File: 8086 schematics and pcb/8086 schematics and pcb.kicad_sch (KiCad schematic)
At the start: 0 parts

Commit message: first test of schmatic bus and PCB concept
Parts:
- added BUS1: 8086 BUS, Package_DIP:SMDIP-64_W15.24mm, symbol 8086PC:8086PC_BUS
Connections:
- new net AD0: BUS1.1 (AD0)
- new net AD1: BUS1.2 (AD1)
- new net AD2: BUS1.3 (AD2)
- new net AD3: BUS1.4 (AD3)
- new net AD4: BUS1.5 (AD4)
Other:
- added sheet 8086 Module (module_8086.kicad_sch)
- added sheet IO Module (module_io.kicad_sch)
- added sheet Microcontroller Module (module_microcontroller.kicad_sch)
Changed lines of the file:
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@@
     (date "2023.08.23")
   )
-  (bus_alias "8086BUS" (members "V_{CC}" "GND" "ADDRESS_LATCHED[0..19]" "DATA[0..15]"))
+  (bus_alias "8086BUS" (members "5V" "GND" "3V3" "AD[0..15]" "A[16..19]" "~{RD}" "~{WR}" "~{BHE}" "ALE" "CLK" "RESET" "HLDA" "HLDA" "~{INTA}" "INTR" "NMI" "~{TEST}" "READY" "~{IO[0..7]}" "~{SEG[2..7]}"))
+  (bus_entry (at 127 35.56) (size 2.54 -2.54)
+    (stroke (width 0) (type default))
+  )
+  (bus_entry (at 127 45.72) (size 2.54 -2.54)
+    (stroke (width 0) (type default))
+  )
+  (bus_entry (at 127 38.1) (size 2.54 -2.54)
+    (stroke (width 0) (type default))
+  )
+  (bus_entry (at 127 40.64) (size 2.54 -2.54)
+    (stroke (width 0) (type default))
+  )
+  (bus_entry (at 127 48.26) (size 2.54 -2.54)
+    (stroke (width 0) (type default))
+  )
+  (wire (pts (xy 137.16 35.56) (xy 137.16 33.02))
+    (stroke (width 0) (type default))
+  )
+  (wire (pts (xy 129.54 43.18) (xy 137.16 43.18))
+    (stroke (width 0) (type default))
+  )
+  (wire (pts (xy 129.54 45.72) (xy 137.16 45.72))
+    (stroke (width 0) (type default))
+  )
+  (bus (pts (xy 170.18 102.87) (xy 173.99 102.87))
+    (stroke (width 0) (type default))
+  )
+  (wire (pts (xy 132.08 38.1) (xy 132.08 40.64))
+    (stroke (width 0) (type default))
+  )
+  (bus (pts (xy 127 40.64) (xy 127 45.72))
+    (stroke (width 0) (type default))
+  )
+  (wire (pts (xy 129.54 35.56) (xy 134.62 35.56))
+    (stroke (width 0) (type default))
+  )
+  (bus (pts (xy 127 45.72) (xy 127 48.26))
+    (stroke (width 0) (type default))
+  )
+  (bus (pts (xy 127 48.26) (xy 127 121.92))
+    (stroke (width 0) (type default))
+  )
+  (wire (pts (xy 134.62 35.56) (xy 134.62 38.1))
+    (stroke (width 0) (type default))
+  )
+  (bus (pts (xy 127 38.1) (xy 127 40.64))
+    (stroke (width 0) (type default))
+  )
+  (bus (pts (xy 127 25.4) (xy 127 35.56))
+    (stroke (width 0) (type default))
+  )
+  (bus (pts (xy 170.18 25.4) (xy 127 25.4))
+    (stroke (width 0) (type default))
+  )
+  (bus (pts (xy 170.18 102.87) (xy 170.18 25.4))
+    (stroke (width 0) (type default))
+  )
+  (wire (pts (xy 129.54 33.02) (xy 137.16 33.02))
+    (stroke (width 0) (type default))
+  )
+  (bus (pts (xy 127 35.56) (xy 127 38.1))
+    (stroke (width 0) (type default))
+  )
+  (wire (pts (xy 134.62 38.1) (xy 137.16 38.1))
+    (stroke (width 0) (type default))
+  )
+  (wire (pts (xy 132.08 40.64) (xy 137.16 40.64))
+    (stroke (width 0) (type default))
+  )
+  (wire (pts (xy 129.54 38.1) (xy 132.08 38.1))
+    (stroke (width 0) (type default))
+  )
+  (label "AD4" (at 129.54 45.72 0)
+    (effects (font (size 1.27 1.27)) (justify left bottom))
+  )
+  (label "AD2" (at 132.08 40.64 0)
+    (effects (font (size 1.27 1.27)) (justify left bottom))
+  )
+  (label "AD0" (at 135.89 33.02 0)
+    (effects (font (size 1.27 1.27)) (justify left bottom))
+  )
+  (label "AD3" (at 132.08 43.18 0)
+    (effects (font (size 1.27 1.27)) (justify left bottom))
+  )
+  (label "AD1" (at 137.16 38.1 0)
+    (effects (font (size 1.27 1.27)) (justify left bottom))
+  )
+  (global_label "{8086BUS}" (shape input) (at 173.99 102.87 0) (fields_autoplaced)
+    (effects (font (size 1.27 1.27)) (justify left))
+    (property "Intersheetrefs" "${INTERSHEET_REFS}" (at 187.2372 102.87 0)
+      (effects (font (size 1.27 1.27)) (justify left) hide)
+    )
+  )
+  (symbol (lib_id "8086PC:8086PC_BUS") (at 149.86 78.74 0) (unit 1)
+    (in_bom yes) (on_board yes) (dnp no)
+    (property "Reference" "BUS1" (at 149.86 78.74 0)
+      (effects (font (size 1.27 1.27)) hide)
+    )
+    (property "Value" "8086 BUS" (at 149.86 78.74 0)
+      (effects (font (size 1.27 1.27)))
+    )
+    (property "Footprint" "Package_DIP:SMDIP-64_W15.24mm" (at 160.02 49.53 0)
+      (effects (font (size 1.27 1.27)) hide)
+    )
+    (property "Datasheet" "" (at 160.02 49.53 0)
+      (effects (font (size 1.27 1.27)) hide)
+    )
+    (pin "1")
+    (pin "10")
+    (pin "11")
+    (pin "12")
+    (pin "13")
+    (pin "14")
+    (pin "15")
+    (pin "16")
+    (pin "17")
+    (pin "18")
+    (pin "19")
+    (pin "2")
+    (pin "20")
+    (pin "26")
+    (pin "27")
+    (pin "28")
+    (pin "29")
+    (pin "3")
+    (pin "30")
+    (pin "31")
+    (pin "32")
+    (pin "4")
+    (pin "49")
+    (pin "5")
+    (pin "50")
+    (pin "51")
+    (pin "52")
+    (pin "53")
+    (pin "54")
+    (pin "55")
+    (pin "56")
+    (pin "6")
+    (pin "7")
+    (pin "8")
+    (pin "9")
+    (pin "21")
+    (pin "22")
+    (pin "23")
+    (pin "24")
+    (pin "25")
+    (pin "33")
+    (pin "34")
+    (pin "35")
+    (pin "36")
+    (pin "37")
+    (pin "38")
+    (pin "39")
+    (pin "40")
+    (pin "41")
+    (pin "42")
+    (pin "43")
+    (pin "44")
+    (pin "45")
+    (pin "46")
+    (pin "47")
+    (pin "48")
+    (instances
+      (project "8086 schematics and pcb"
+        (path "/3749a875-289f-4484-aa3f-51b8984af853"
+          (reference "BUS1") (unit 1)
+        )
+      )
+    )
+  )
+  (sheet (at 25.4 137.16) (size 76.2 50.8) (fields_autoplaced)
+    (stroke (width 0.1524) (type solid))
+    (fill (color 0 0 0 0.0000))
+    (property "Sheetname" "Microcontroller Module" (at 25.4 136.4484 0)
+      (effects (font (size 1.27 1.27)) (justify left bottom))
+    )
+    (property "Sheetfile" "module_microcontroller.kicad_sch" (at 25.4 188.5446 0)
+      (effects (font (size 1.27 1.27)) (justify left top))
+    )
+    (instances
+      (project "8086 schematics and pcb"
+        (path "/3749a875-289f-4484-aa3f-51b8984af853" (page "4"))
+      )
+    )
+  )
+  (sheet (at 25.4 25.4) (size 76.2 50.8) (fields_autoplaced)
+    (stroke (width 0.1524) (type solid))
+    (fill (color 0 0 0 0.0000))
+    (property "Sheetname" "8086 Module" (at 25.4 24.6884 0)
+      (effects (font (size 1.27 1.27)) (justify left bottom))
+    )
+    (property "Sheetfile" "module_8086.kicad_sch" (at 25.4 76.7846 0)
+      (effects (font (size 1.27 1.27)) (justify left top))
+    )
+    (instances
+      (project "8086 schematics and pcb"
+        (path "/3749a875-289f-4484-aa3f-51b8984af853" (page "2"))
+      )
+    )
+  )
+  (sheet (at 25.4 81.28) (size 76.2 50.8) (fields_autoplaced)
+    (stroke (width 0.1524) (type solid))
+    (fill (color 0 0 0 0.0000))
+    (property "Sheetname" "IO Module" (at 25.4 80.5684 0)
+      (effects (font (size 1.27 1.27)) (justify left bottom))
+    )
+    (property "Sheetfile" "module_io.kicad_sch" (at 25.4 132.6646 0)
+      (effects (font (size 1.27 1.27)) (justify left top))
+    )
+    (instances
+      (project "8086 schematics and pcb"
+        (path "/3749a875-289f-4484-aa3f-51b8984af853" (page "3"))
+      )
+    )
+  )
   (sheet_instances
     (path "/" (page "1"))

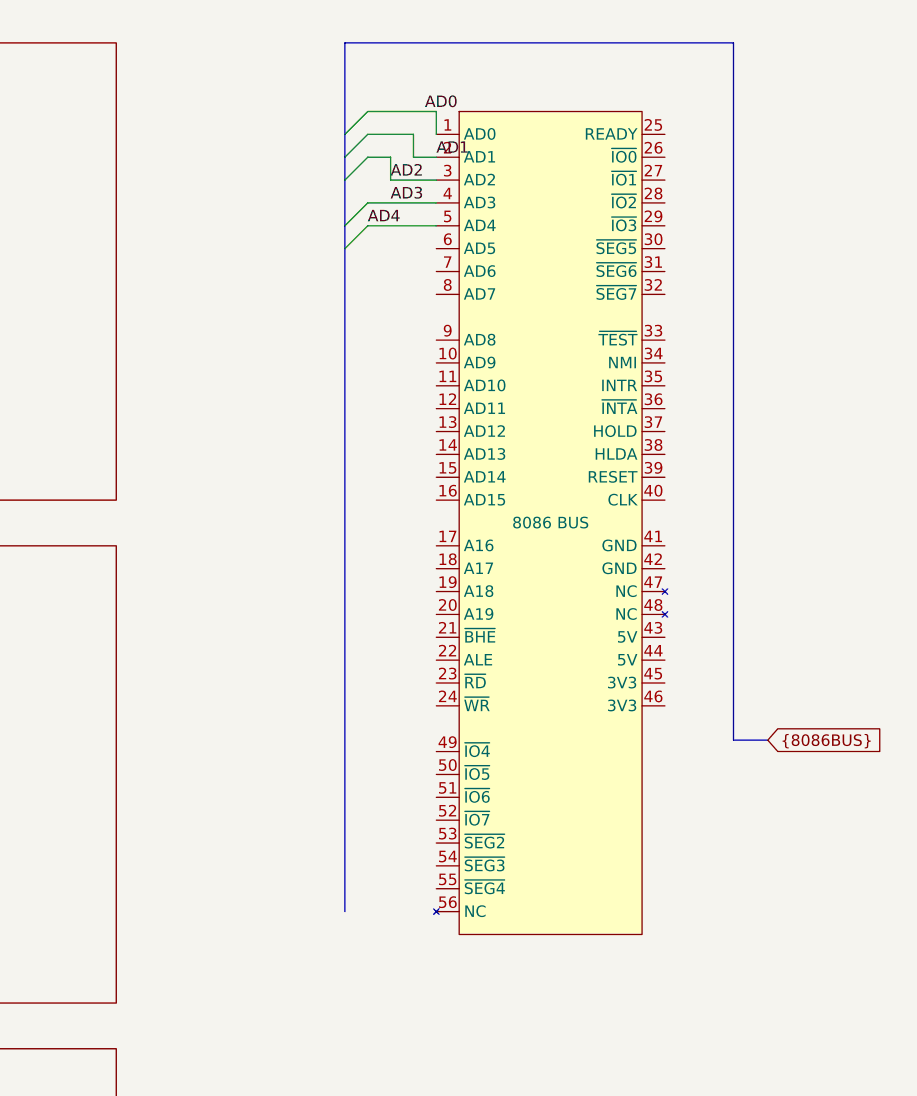
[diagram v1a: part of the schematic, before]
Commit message: 8086 module - bus connected
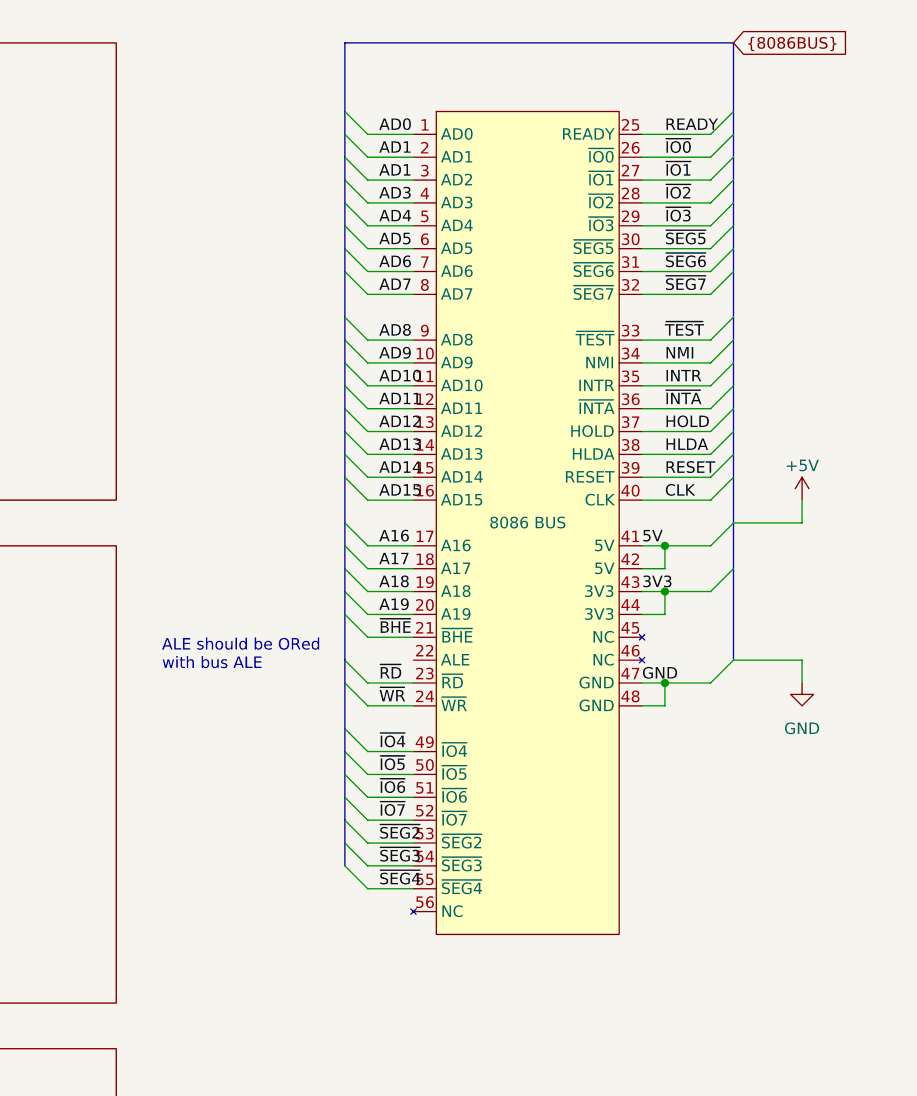
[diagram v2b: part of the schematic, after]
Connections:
- net AD2 is gone; now on net AD1: BUS1.3 (AD2)
- net AD9: now reaches BUS1.10 (AD9)
- net AD10: now reaches BUS1.11 (AD10)
- net AD11: now reaches BUS1.12 (AD11)
- net AD12: now reaches BUS1.13 (AD12)
- net AD13: now reaches BUS1.14 (AD13)
- net AD14: now reaches BUS1.15 (AD14)
- net AD15: now reaches BUS1.16 (AD15)
- net A16: now reaches BUS1.17 (A16)
- net A17: now reaches BUS1.18 (A17)
- net A18: now reaches BUS1.19 (A18)
- net A19: now reaches BUS1.20 (A19)
- net ~{BHE}: now reaches BUS1.21 (~{BHE})
- net ~{RD}: now reaches BUS1.23 (~{RD})
- net ~{WR}: now reaches BUS1.24 (~{WR})
- net READY: now reaches BUS1.25 (READY)
- net ~{IO0}: now reaches BUS1.26 (~{IO0})
- net ~{IO1}: now reaches BUS1.27 (~{IO1})
- net ~{IO2}: now reaches BUS1.28 (~{IO2})
- net ~{IO3}: now reaches BUS1.29 (~{IO3})
- net ~{SEG5}: now reaches BUS1.30 (~{SEG5})
- net ~{SEG6}: now reaches BUS1.31 (~{SEG6})
- net ~{SEG7}: now reaches BUS1.32 (~{SEG7})
- net ~{TEST}: now reaches BUS1.33 (~{TEST})
- net NMI: now reaches BUS1.34 (NMI)
- net INTR: now reaches BUS1.35 (INTR)
- net ~{INTA}: now reaches BUS1.36 (~{INTA})
- net HOLD: now reaches BUS1.37 (HOLD)
- net HLDA: now reaches BUS1.38 (HLDA)
- net RESET: now reaches BUS1.39 (RESET)
- net CLK: now reaches BUS1.40 (CLK)
- net 5V: now reaches BUS1.41 (5V)
- net 5V: now also BUS1.42 (5V)
- net 3V3: now reaches BUS1.43 (3V3)
- net 3V3: now also BUS1.44 (3V3)
- net GND: now reaches BUS1.47 (GND)
- net GND: now also BUS1.48 (GND)
- net ~{IO4}: now reaches BUS1.49 (~{IO4})
- net ~{IO5}: now reaches BUS1.50 (~{IO5})
- net ~{IO6}: now reaches BUS1.51 (~{IO6})
- net ~{IO7}: now reaches BUS1.52 (~{IO7})
- net ~{SEG2}: now reaches BUS1.53 (~{SEG2})
- net ~{SEG3}: now reaches BUS1.54 (~{SEG3})
- net ~{SEG4}: now reaches BUS1.55 (~{SEG4})
- net AD5: now reaches BUS1.6 (AD5)
- net AD6: now reaches BUS1.7 (AD6)
- net AD7: now reaches BUS1.8 (AD7)
- net AD8: now reaches BUS1.9 (AD8)
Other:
- note added: "ALE should be ORed with bus ALE"

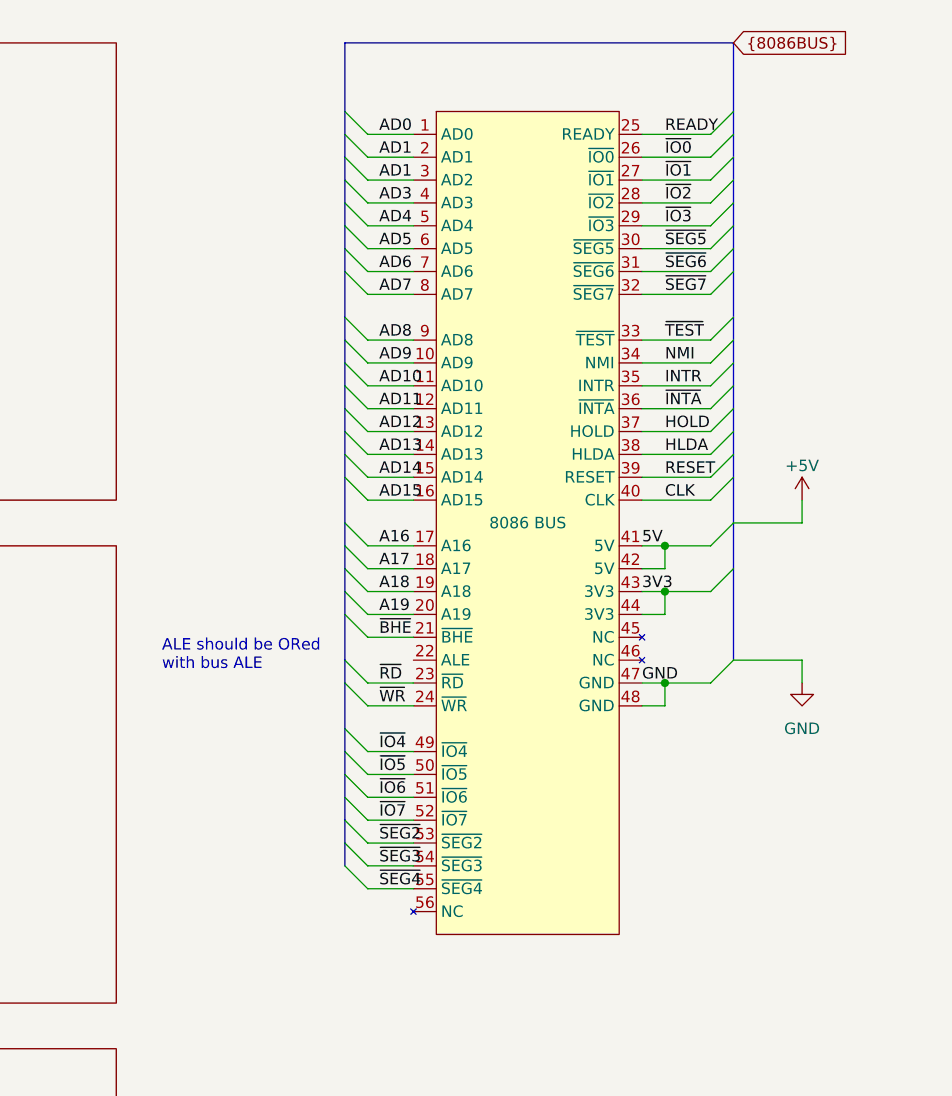
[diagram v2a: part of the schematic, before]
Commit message: - changed SEG and IO pins to bidirectional - added "Local to Module" netclass.
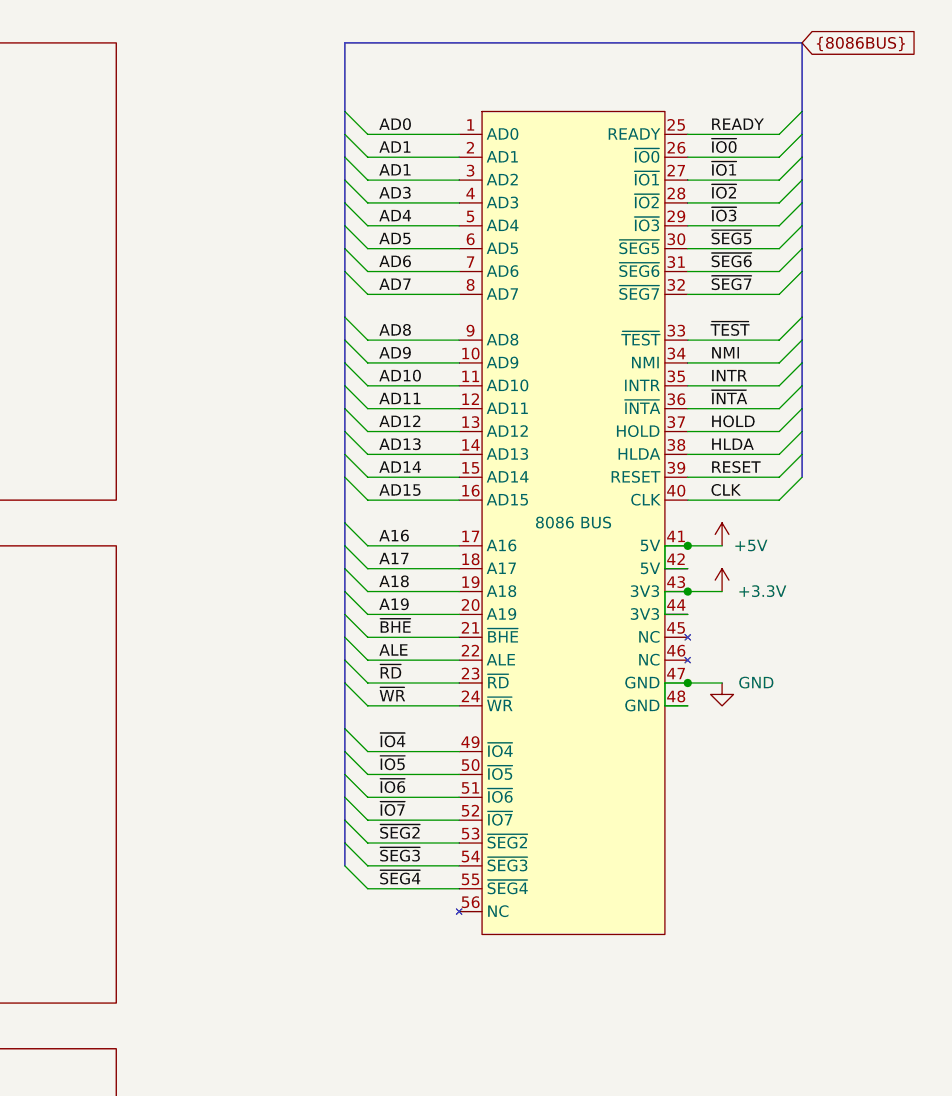
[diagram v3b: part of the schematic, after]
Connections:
- net 5V is gone; now on net +5V: BUS1.41 (5V), BUS1.42 (5V)
- net ALE: now reaches BUS1.22 (ALE)
- net 3V3 renamed +3.3V
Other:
- note removed: "ALE should be ORed with bus ALE"

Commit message: basic start for IO module
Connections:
- net ALE renamed BUSALE
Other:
- sheet 8086 Module renamed 8086 Module - 1
- added sheet 8086 Module - 2 (module_8086_2.kicad_sch)
- sheet 8086 Module - 1: file module_8086.kicad_sch -> module_8086_1.kicad_sch
- sheet 8086 Module - 1 ports: added LA[0..19], ~{LA19}, ~{LBHE}, ~{MEM1H}, ~{MEM1L}, ~{SEG0H}, ~{SEG0L}, ~{SEG0}, ~{SEG1}; removed none
- note added: "8086 and logic IC's"
- note added: "Memory IC's"
